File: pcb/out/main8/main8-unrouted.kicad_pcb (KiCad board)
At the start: 2 copper layers, 202.8 x 148.8 mm, 120 parts, among them K1 RX1, K2 RX2, K3 RX3, K4 RX4, K5 RX5, K6 RX6, K7 RX7, K8 RX8, T1 TX1, T2 TX2, T3 TX3, U1 74HCT04, U2 MCP6024, U3 MCP6024, U4 MCP6024, U5 MCP6024, U6 MCP6024

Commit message: pcb: ใช้เบอร์ชิ้นส่วนที่สั่งซื้อได้จริง และเขียนหมายเหตุการประกอบลง BOM
BOM เดิมเขียนชื่อกว้าง ๆ เอาไปสั่งซื้อตรง ๆ ไม่ได้
  74HCT04   -> SN74HCT04N
  MCP6024   -> MCP6024-I/P     (ตัวถัง DIP ต้องเป็นรหัส -I/P)
  Blue Pill -> 1x20 female hdr (ของที่บัดกรีคือเฮดเดอร์ ไม่ใช่บอร์ด STM32)

เพิ่มหมายเหตุที่ต้องรู้ตอนซื้อและตอนประกอบไว้ในไฟล์ BOM ของบอร์ดนั้นเลย
จะได้ไม่ต้องถือเอกสารสองใบตอนไปร้าน เรื่องสำคัญคือให้ซื้อซ็อกเก็ต DIP-14
มาใส่แทนการบัดกรีชิปลงบอร์ดตรง ๆ รูเหมือนกันเป๊ะไม่ต้องแก้บอร์ด

แก้จุดที่จะทำให้เอกสารค้างรุ่นเก่าโดยไม่มีใครรู้ด้วย: main8 ให้ EasyEDA
เดินลายจึงออกทาง unrouted() ไม่ได้ผ่าน build() ซึ่งเป็นที่เดียวที่เขียน
BOM.md กับ nets.md แก้ให้ unrouted() เขียนเอกสารทั้งสองด้วย

ตัวบอร์ดไม่เปลี่ยน ทองแดงและรูเหมือนเดิมทุกจุด แก้เฉพาะข้อความ
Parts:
- JA, JB: value Blue Pill -> 1x20 female hdr
- U1: value 74HCT04 -> SN74HCT04N
- U2, U3, U4, U5, U6: value MCP6024 -> MCP6024-I/P
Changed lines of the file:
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@@
     (attr through_hole)
     (fp_text reference "JA" (at 0 -2.2) (layer "F.SilkS") (effects (font (size 1 1) (thickness 0.15))))
-    (fp_text value "Blue Pill" (at 0 2.2) (layer "F.Fab") (effects (font (size 1 1) (thickness 0.15))))
+    (fp_text value "1x20 female hdr" (at 0 2.2) (layer "F.Fab") (effects (font (size 1 1) (thickness 0.15))))
     (pad "1" thru_hole rect (at 0.0 0.0) (size 1.8 1.8) (drill 1.0) (layers "*.Cu" "*.Mask") (net 1 "GND"))
     (pad "2" thru_hole circle (at 2.54 0.0) (size 1.8 1.8) (drill 1.0) (layers "*.Cu" "*.Mask") (net 1 "GND"))
@@
     (attr through_hole)
     (fp_text reference "JB" (at 0 -2.2) (layer "F.SilkS") (effects (font (size 1 1) (thickness 0.15))))
-    (fp_text value "Blue Pill" (at 0 2.2) (layer "F.Fab") (effects (font (size 1 1) (thickness 0.15))))
+    (fp_text value "1x20 female hdr" (at 0 2.2) (layer "F.Fab") (effects (font (size 1 1) (thickness 0.15))))
     (pad "1" thru_hole rect (at 0.0 0.0) (size 1.8 1.8) (drill 1.0) (layers "*.Cu" "*.Mask") (net 100 "NC_JB_B12"))
     (pad "2" thru_hole circle (at 2.54 0.0) (size 1.8 1.8) (drill 1.0) (layers "*.Cu" "*.Mask") (net 101 "NC_JB_B13"))
@@
     (attr through_hole)
     (fp_text reference "U1" (at 0 -2.2) (layer "F.SilkS") (effects (font (size 1 1) (thickness 0.15))))
-    (fp_text value "74HCT04" (at 0 2.2) (layer "F.Fab") (effects (font (size 1 1) (thickness 0.15))))
+    (fp_text value "SN74HCT04N" (at 0 2.2) (layer "F.Fab") (effects (font (size 1 1) (thickness 0.15))))
     (pad "1" thru_hole rect (at 0.0 0.0) (size 1.7 1.7) (drill 0.9) (layers "*.Cu" "*.Mask") (net 11 "TX1_IN"))
     (pad "2" thru_hole circle (at 2.54 0.0) (size 1.7 1.7) (drill 0.9) (layers "*.Cu" "*.Mask") (net 15 "TX1_MID"))
@@
     (attr through_hole)
     (fp_text reference "U2" (at 0 -2.2) (layer "F.SilkS") (effects (font (size 1 1) (thickness 0.15))))
-    (fp_text value "MCP6024" (at 0 2.2) (layer "F.Fab") (effects (font (size 1 1) (thickness 0.15))))
+    (fp_text value "MCP6024-I/P" (at 0 2.2) (layer "F.Fab") (effects (font (size 1 1) (thickness 0.15))))
     (pad "1" thru_hole rect (at 0.0 0.0) (size 1.7 1.7) (drill 0.9) (layers "*.Cu" "*.Mask") (net 27 "RX1_S1O"))
     (pad "2" thru_hole circle (at 2.54 0.0) (size 1.7 1.7) (drill 0.9) (layers "*.Cu" "*.Mask") (net 28 "RX1_S1N"))
@@
     (attr through_hole)
     (fp_text reference "U3" (at 0 -2.2) (layer "F.SilkS") (effects (font (size 1 1) (thickness 0.15))))
-    (fp_text value "MCP6024" (at 0 2.2) (layer "F.Fab") (effects (font (size 1 1) (thickness 0.15))))
+    (fp_text value "MCP6024-I/P" (at 0 2.2) (layer "F.Fab") (effects (font (size 1 1) (thickness 0.15))))
     (pad "1" thru_hole rect (at 0.0 0.0) (size 1.7 1.7) (drill 0.9) (layers "*.Cu" "*.Mask") (net 43 "RX3_S1O"))
     (pad "2" thru_hole circle (at 2.54 0.0) (size 1.7 1.7) (drill 0.9) (layers "*.Cu" "*.Mask") (net 44 "RX3_S1N"))
@@
     (attr through_hole)
     (fp_text reference "U4" (at 0 -2.2) (layer "F.SilkS") (effects (font (size 1 1) (thickness 0.15))))
-    (fp_text value "MCP6024" (at 0 2.2) (layer "F.Fab") (effects (font (size 1 1) (thickness 0.15))))
+    (fp_text value "MCP6024-I/P" (at 0 2.2) (layer "F.Fab") (effects (font (size 1 1) (thickness 0.15))))
     (pad "1" thru_hole rect (at 0.0 0.0) (size 1.7 1.7) (drill 0.9) (layers "*.Cu" "*.Mask") (net 59 "RX5_S1O"))
     (pad "2" thru_hole circle (at -2.54 0.0) (size 1.7 1.7) (drill 0.9) (layers "*.Cu" "*.Mask") (net 60 "RX5_S1N"))
@@
     (attr through_hole)
     (fp_text reference "U5" (at 0 -2.2) (layer "F.SilkS") (effects (font (size 1 1) (thickness 0.15))))
-    (fp_text value "MCP6024" (at 0 2.2) (layer "F.Fab") (effects (font (size 1 1) (thickness 0.15))))
+    (fp_text value "MCP6024-I/P" (at 0 2.2) (layer "F.Fab") (effects (font (size 1 1) (thickness 0.15))))
     (pad "1" thru_hole rect (at 0.0 0.0) (size 1.7 1.7) (drill 0.9) (layers "*.Cu" "*.Mask") (net 75 "RX7_S1O"))
     (pad "2" thru_hole circle (at -2.54 0.0) (size 1.7 1.7) (drill 0.9) (layers "*.Cu" "*.Mask") (net 76 "RX7_S1N"))
@@
     (attr through_hole)
     (fp_text reference "U6" (at 0 -2.2) (layer "F.SilkS") (effects (font (size 1 1) (thickness 0.15))))
-    (fp_text value "MCP6024" (at 0 2.2) (layer "F.Fab") (effects (font (size 1 1) (thickness 0.15))))
+    (fp_text value "MCP6024-I/P" (at 0 2.2) (layer "F.Fab") (effects (font (size 1 1) (thickness 0.15))))
     (pad "1" thru_hole rect (at 0.0 0.0) (size 1.7 1.7) (drill 0.9) (layers "*.Cu" "*.Mask") (net 90 "VREF"))
     (pad "2" thru_hole circle (at 2.54 0.0) (size 1.7 1.7) (drill 0.9) (layers "*.Cu" "*.Mask") (net 90 "VREF"))

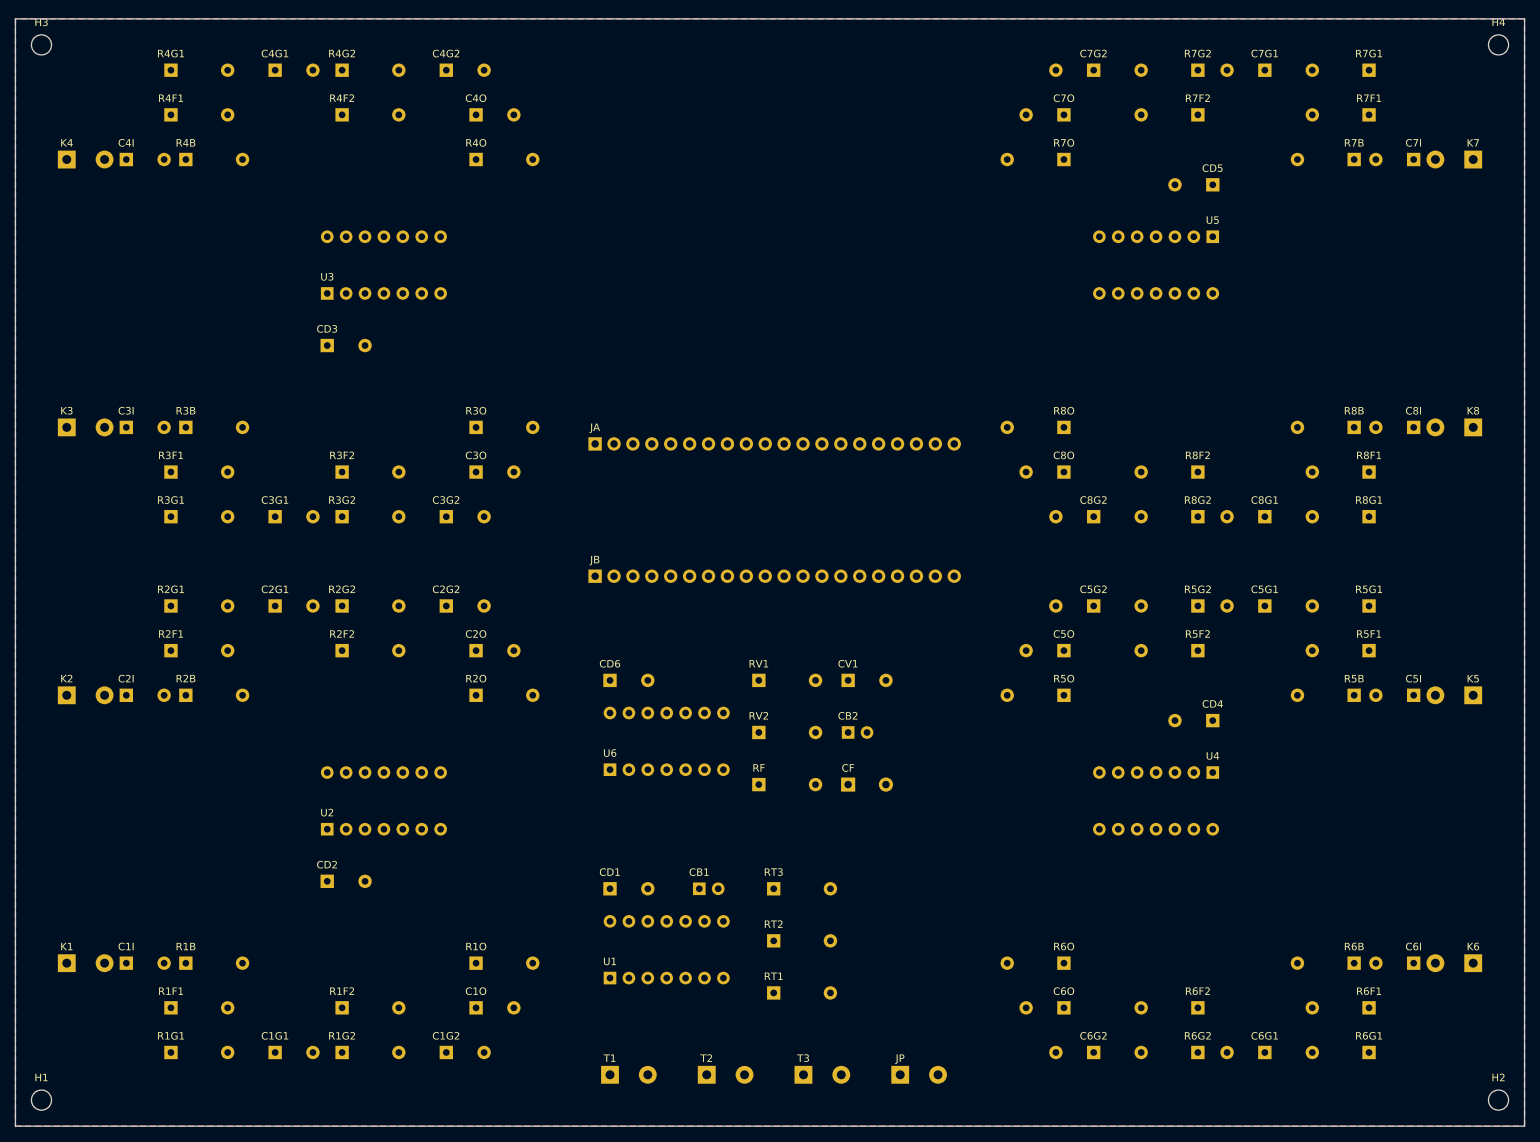
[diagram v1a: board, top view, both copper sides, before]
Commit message: pcb: แก้ผังที่นำเข้าแล้วแตกเป็นเส้น เพิ่มกรอบตัวถังบนบอร์ด และแพ็คเป็นซิป
**สาเหตุที่ผังเปิดใน EasyEDA แล้วเป็นเส้นลอย ๆ ไม่เป็นสัญลักษณ์**
ตัวต้านทานแนวนอน แนวตั้ง และแบบสลับขา ถูกยัดให้ใช้นิยามสัญลักษณ์ตัวเดียวกัน
ตัวที่บันทึกทีหลังทับตัวก่อนหน้า ขาของอีกสามทิศจึงไปโผล่ผิดที่ สายกับขา
ไม่บรรจบกัน โดนแบบนี้ 54 ตัวจาก 142 (คาปาและเทอร์มินอลก็เป็นแบบเดียวกัน)
แยกนิยามตามทิศของขา 1 แล้วใส่ตัวกันไว้ ถ้าชื่อเดียวกันถูกใช้กับสองรูปทรงจะหยุดทันที

**เพิ่มตัวตรวจพิกัด ซึ่งจับบั๊กข้างบนได้ตั้งแต่แรกถ้ามีมาก่อน**
ตัวตรวจเดิมดูว่า "ขาไหนควรอยู่เน็ตอะไร" ซึ่งผ่านหมดทั้ง 340 ขา
แต่ไม่ได้ดูว่า "สายไปบรรจบกับขาตรงพิกัดจริงหรือเปล่า"
ตัวใหม่จับได้ 50 ขาลอย ในนั้นมีรอยขาดจริงในผังด้วย ซึ่งภาพ SVG ก็ขาดตามไปด้วย
  ขาซ้ายของตัวป้อนกลับไม่ได้ต่อกับปมขาลบ (ทั้ง 16 สเตจ)
  คาปาปลายทางกับคาปากรองไฟไม่ได้ต่อกับปมที่ห้อยอยู่
เติมสายที่ขาดแล้ว ตอนนี้ทุกขาใน 340 จุดมีสายหรือป้ายมาบรรจบจริง
ขาที่ตั้งใจไม่ต่อ 23 ขา ใส่เครื่องหมายไม่ต่อให้ ไม่ให้โปรแกรมเตือนว่าลืม

**หน้ากระดาษ** เดิมเรียงทุกแผ่นลงล่างจนได้ 503 x 1956 มม. เปิดมาเป็นแถบผอม
เปลี่ยนเป็นวางเป็นคอลัมน์ และภาครับ 8 ช่องวางเป็นตาราง 2x4
ได้ 1386 x 766 มม. สัดส่วนใกล้เคียงกระดาษปกติ

**บอร์ดไม่มีเส้นกรอบตัวถังเลยแม้แต่เส้นเดียว** มีแต่แป้นกับตัวอักษร
geom.body() มีมานานแล้วแต่ตัวส่งออก KiCad ไม่เคยเรียกใช้
ประกอบไม่ได้เพราะมองไม่ออกว่าตัวไหนหันทางไหน และ 3D ก็โล่งเพราะไม่มีอะไรให้วาด
เพิ่มกรอบ 464 เส้น (116 ตัว x 4 ด้าน) และจุดบอกขา 1 ทุกตัว

**pack_kicad()** แพ็ค .kicad_pro + .kicad_sch + .kicad_pcb เป็นซิปเดียว
ชื่อไฟล์ทั้งสามต้องตรงกัน ตัวนำเข้าจึงจะผูกผังกับบอร์ดเข้าด้วยกันได้
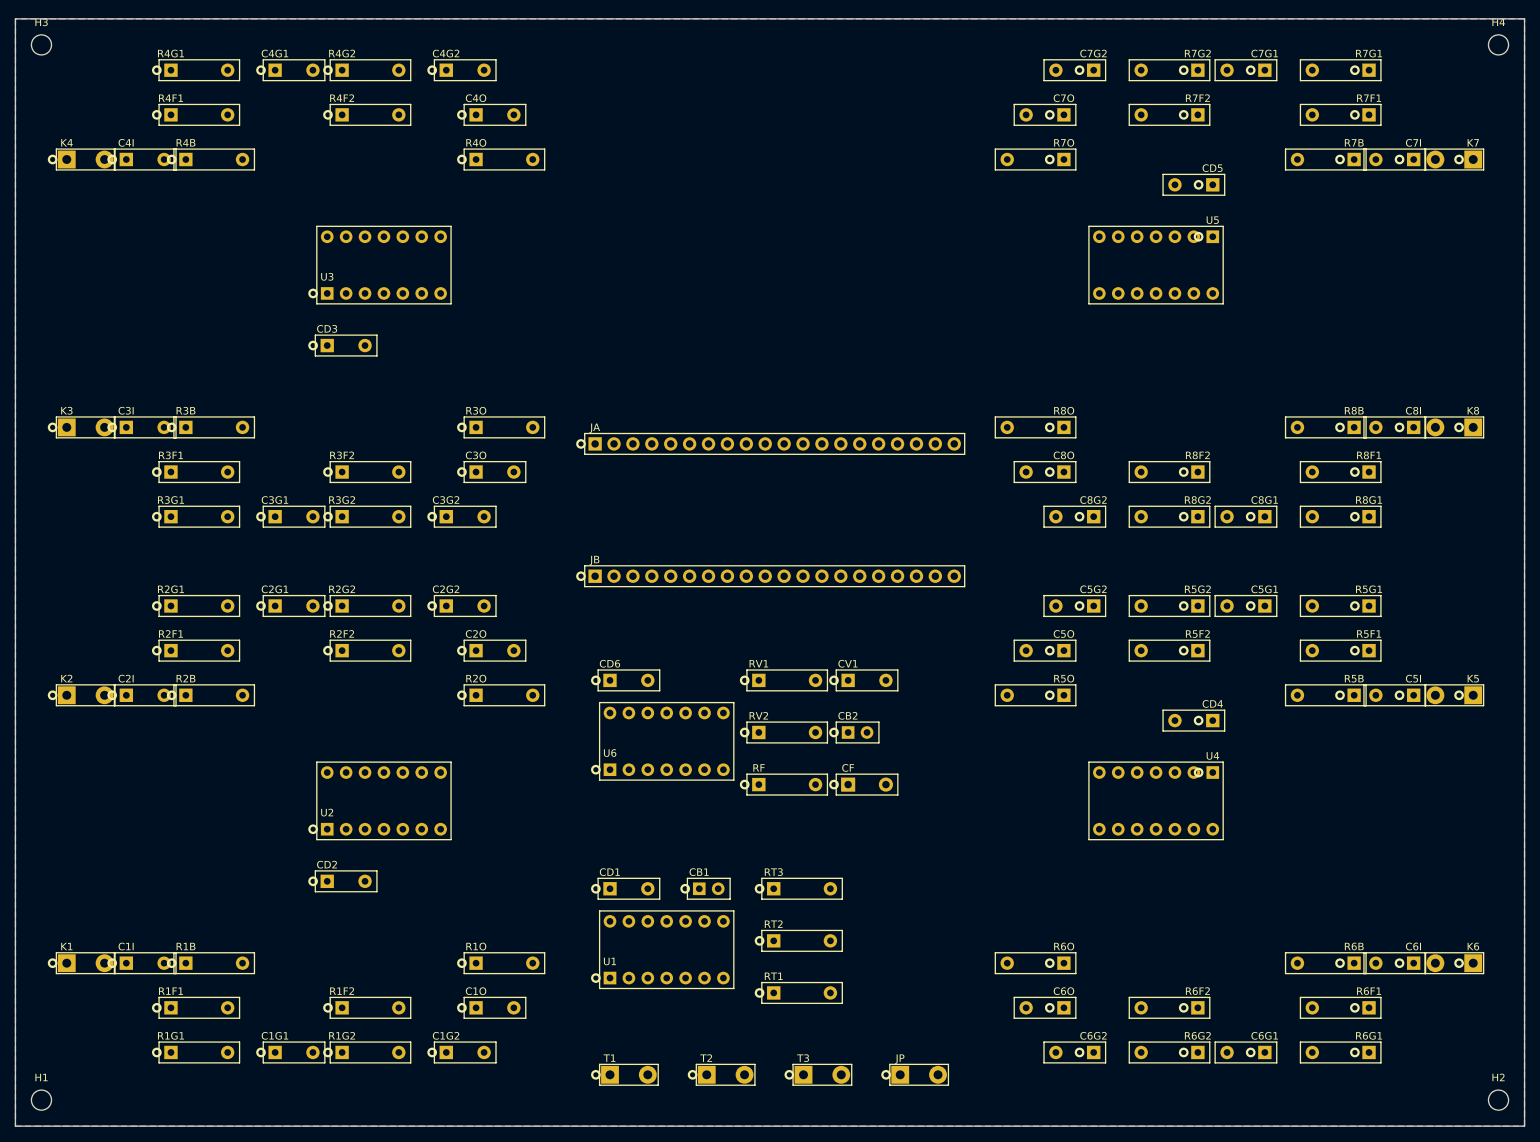
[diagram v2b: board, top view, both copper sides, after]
